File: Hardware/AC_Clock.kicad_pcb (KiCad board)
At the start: 2 copper layers, 132.1 x 100.3 mm, 71 parts, among them J1 L, J2 N, J3 Conn_01x10, J4 Conn_01x10, J5 Conn_01x10, J6 Conn_01x10, SW1 Min_PB, SW2 Hr_PB, T1 10:1, U1 AZ1117-5.0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

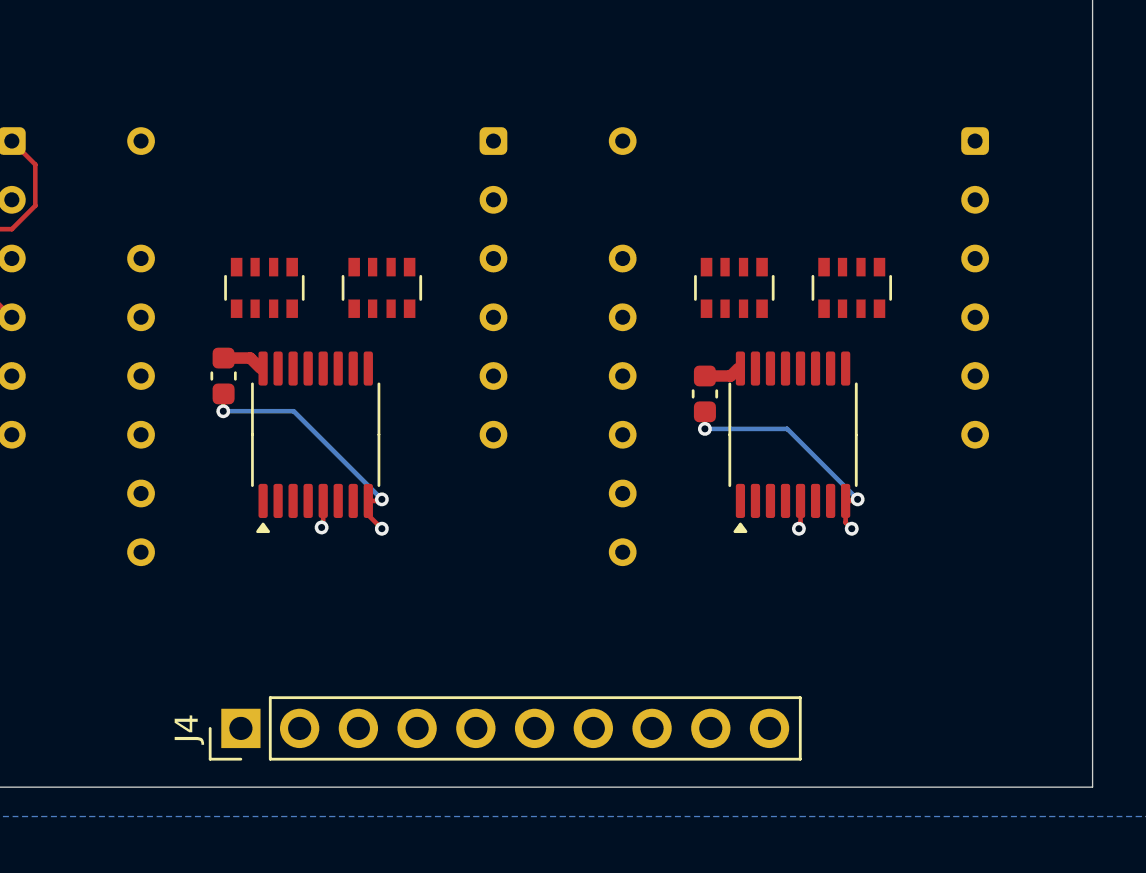
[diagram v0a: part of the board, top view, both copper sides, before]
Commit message: Route the 10/hours digits. Update HDSP-816E footprint to include 3D representation
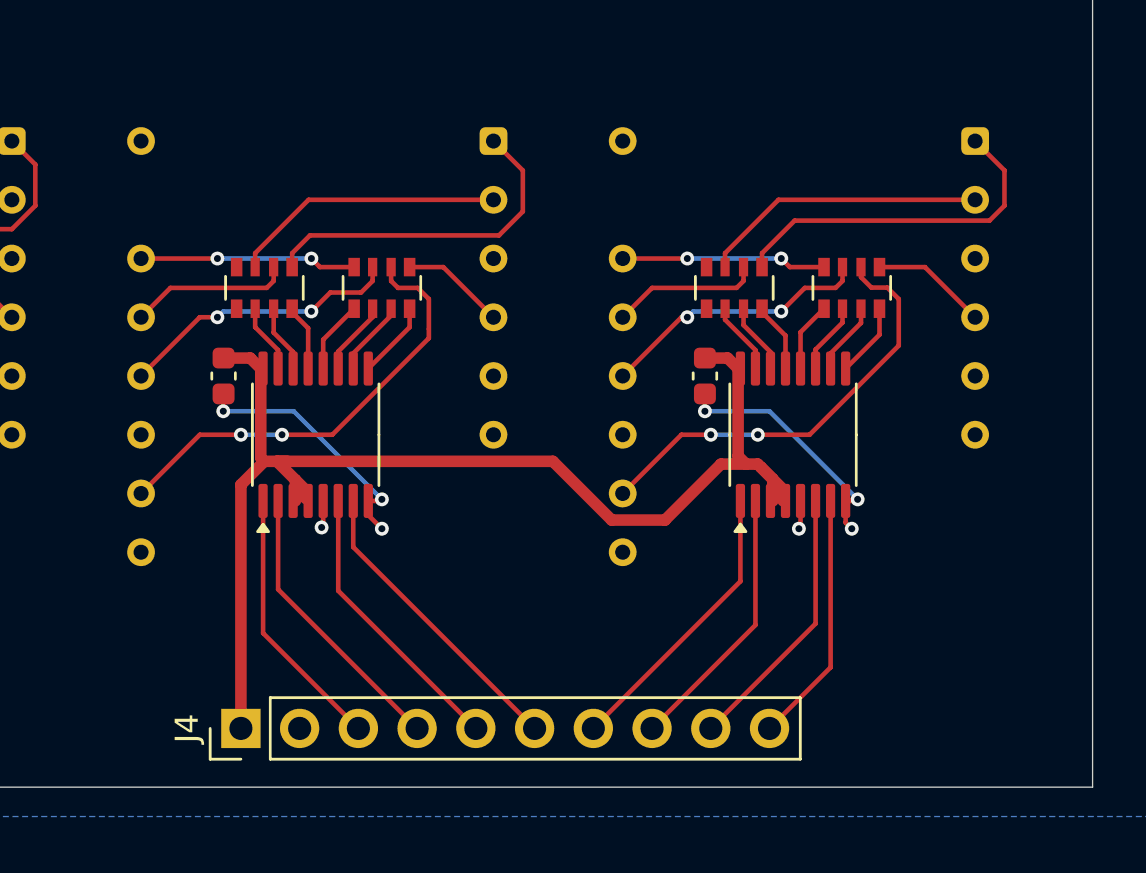
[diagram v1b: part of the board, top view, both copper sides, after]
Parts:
- moved C9 0.78 mm to (148.3, 64.8)
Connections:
- RN7 pad 2: unconnected-(RN7B-R2.1-Pad2) -> Net-(RN7B-R2.1)
- U12 pad 15: unconnected-(U12-Qf-Pad15) -> Net-(RN7B-R2.1)
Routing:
- net +5V: track 204.1 -> 255.1 mm
- net Net-(RN6-R3.2): track 0.00 -> 19.5 mm, vias 0 -> 2
- net Net-(RN8-R3.2): track 0.00 -> 19.1 mm, vias 0 -> 2
- net Net-(RN7D-R4.2): track 0.00 -> 15.3 mm
- net Net-(RN5D-R4.2): track 0.00 -> 14.9 mm
- net DA_3: track 6.38 -> 19.5 mm
- net DB_4: track 0.00 -> 12.5 mm
- net Net-(RN7B-R2.2): track 0.00 -> 12.4 mm
- net DC_3: track 0.00 -> 12.3 mm
- net Net-(RN6-R2.2): track 0.00 -> 12.3 mm, vias 0 -> 2
- net DD_3: track 3.12 -> 15.4 mm
- net Net-(RN5B-R2.2): track 0.00 -> 11.9 mm
- net Net-(RN8-R2.2): track 0.00 -> 11.8 mm, vias 0 -> 2
- net DD_4: track 0.00 -> 11.7 mm
- net DC_4: track 0.00 -> 11.7 mm
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
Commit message: Finish routing main board
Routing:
- net +5V: track 255.1 -> 319.2 mm, vias 2 -> 4
- net DB_3: track 11.5 -> 54.6 mm, vias 0 -> 1
- net DB_1: track 11.4 -> 48.1 mm, vias 0 -> 1
- net DC_3: track 12.3 -> 48.1 mm, vias 0 -> 1
- net DD_3: track 15.4 -> 49.1 mm, vias 0 -> 1
- net DC_1: track 12.2 -> 45.5 mm, vias 0 -> 1
- net DD_1: track 15.3 -> 45.4 mm, vias 0 -> 1
- net DA_3: track 19.5 -> 48.6 mm, vias 0 -> 1
- net /hour: track 9.21 -> 35.2 mm
- net /RST_{10hr}: track 0.00 -> 20.3 mm
- net DA_1: track 19.3 -> 39.6 mm, vias 0 -> 1
- net DA_2: track 14.8 -> 30.0 mm
- net DB_4: track 12.5 -> 26.7 mm
- net DB_2: track 12.7 -> 26.2 mm, vias 0 -> 1
- net DD_4: track 11.7 -> 24.9 mm
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
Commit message: Add Class Y Safety capacitor
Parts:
- added C10: Safety, Capacitor_THT:C_Disc_D7.5mm_W5.0mm_P7.50mm, F.Cu at (59.8, 109.7)
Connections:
- D5 pad 1: /4Hz -> /2Hz
- T1 pad 10: (no net) -> unconnected-(T1-Pad10)
- T1 pad 9: (no net) -> unconnected-(T1-Pad9)
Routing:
- net /AC_12-: track 14.7 -> 26.6 mm
- net Earth: track 50.4 -> 56.1 mm

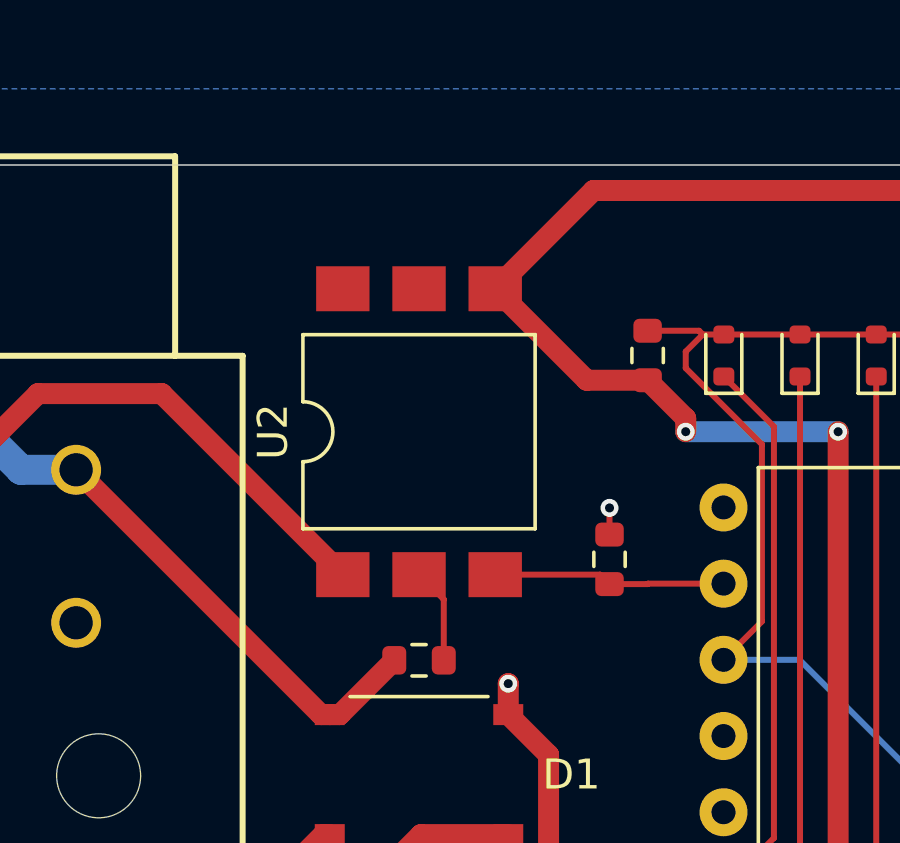
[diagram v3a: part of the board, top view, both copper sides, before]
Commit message: Fix U2 footprint; change to DIP-4
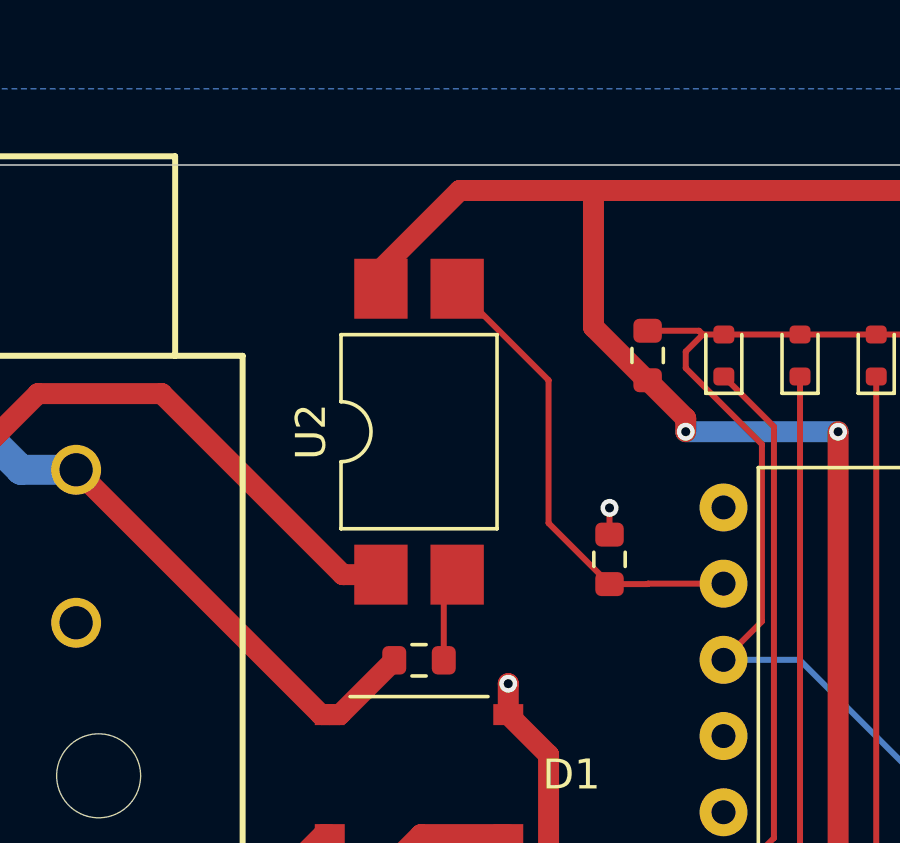
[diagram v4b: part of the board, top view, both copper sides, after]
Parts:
- U2: footprint Package_DIP:SMDIP-6_W9.53mm_Clearance8mm -> Package_DIP:SMDIP-4_W9.53mm
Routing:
- net /Pulse: track 7.75 -> 15.8 mm
- net +5V: track 319.2 -> 324.1 mm
- net /AC_12+: track 50.8 -> 52.1 mm
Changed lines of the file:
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@@
 		)
 	)
-	(footprint "Package_DIP:SMDIP-6_W9.53mm_Clearance8mm"
+	(footprint "Package_DIP:SMDIP-4_W9.53mm"
 		(layer "F.Cu")
 		(at 87.63 115.57 90)
-		(descr "6-lead surface-mounted (SMD) DIP package, row spacing 9.53 mm (375 mils), Clearance8mm")
-		(tags "SMD DIP DIL PDIP SMDIP 2.54mm 9.53mm 375mil Clearance8mm")
+		(descr "4-lead surface-mounted (SMD) DIP package, row spacing 9.53 mm (375 mils)")
+		(tags "SMD DIP DIL PDIP SMDIP 2.54mm 9.53mm 375mil")
 		(property "Reference" "U2"
-			(at 0 -4.87 90)
+			(at 0 -3.6 90)
 			(layer "F.SilkS")
 			(effects
@@
 		)
 		(property "Value" "LTV-817S"
-			(at 0 4.87 90)
+			(at 0 3.6 90)
 			(layer "F.Fab")
 			(effects
@@
 			)
 		)
-		(property "Footprint" "Package_DIP:SMDIP-6_W9.53mm_Clearance8mm"
+		(property "Footprint" "Package_DIP:SMDIP-4_W9.53mm"
 			(at 0 0 90)
 			(unlocked yes)
@@
 		(attr smd)
 		(fp_line
-			(start 3.235 -3.87)
-			(end 1 -3.87)
+			(start 3.235 -2.6)
+			(end 1 -2.6)
 			(stroke
 				(width 0.12)
@@
 		)
 		(fp_line
-			(start -1 -3.87)
-			(end -3.235 -3.87)
+			(start -1 -2.6)
+			(end -3.235 -2.6)
 			(stroke
 				(width 0.12)
@@
 		)
 		(fp_line
-			(start -3.235 -3.87)
-			(end -3.235 3.87)
+			(start -3.235 -2.6)
+			(end -3.235 2.6)
 			(stroke
 				(width 0.12)
@@
 		)
 		(fp_line
-			(start 3.235 3.87)
-			(end 3.235 -3.87)
+			(start 3.235 2.6)
+			(end 3.235 -2.6)
 			(stroke
 				(width 0.12)
@@
 		)
 		(fp_line
-			(start -3.235 3.87)
-			(end 3.235 3.87)
+			(start -3.235 2.6)
+			(end 3.235 2.6)
 			(stroke
 				(width 0.12)
@@
 		)
 		(fp_arc
-			(start 1 -3.87)
-			(mid 0 -2.87)
-			(end -1 -3.87)
+			(start 1 -2.6)
+			(mid 0 -1.6)
+			(end -1 -2.6)
 			(stroke
 				(width 0.12)
@@
 		)
 		(fp_line
-			(start 5.8 -4.1)
-			(end -5.8 -4.1)
+			(start 6.05 -2.8)
+			(end -6.05 -2.8)
 			(stroke
 				(width 0.05)
@@
 		)
 		(fp_line
-			(start -5.8 -4.1)
-			(end -5.8 4.1)
+			(start -6.05 -2.8)
+			(end -6.05 2.8)
 			(stroke
 				(width 0.05)
@@
 		)
 		(fp_line
-			(start 5.8 4.1)
-			(end 5.8 -4.1)
+			(start 6.05 2.8)
+			(end 6.05 -2.8)
 			(stroke
 				(width 0.05)
@@
 		)
 		(fp_line
-			(start -5.8 4.1)
-			(end 5.8 4.1)
+			(start -6.05 2.8)
+			(end 6.05 2.8)
 			(stroke
 				(width 0.05)
@@
 		)
 		(fp_line
-			(start 3.175 -3.81)
-			(end 3.175 3.81)
+			(start 3.175 -2.54)
+			(end 3.175 2.54)
 			(stroke
 				(width 0.1)
@@
 		)
 		(fp_line
-			(start -2.175 -3.81)
-			(end 3.175 -3.81)
+			(start -2.175 -2.54)
+			(end 3.175 -2.54)
 			(stroke
 				(width 0.1)
@@
 		)
 		(fp_line
-			(start -3.175 -2.81)
-			(end -2.175 -3.81)
+			(start -3.175 -1.54)
+			(end -2.175 -2.54)
 			(stroke
 				(width 0.1)
@@
 		)
 		(fp_line
-			(start 3.175 3.81)
-			(end -3.175 3.81)
+			(start 3.175 2.54)
+			(end -3.175 2.54)
 			(stroke
 				(width 0.1)
@@
 		)
 		(fp_line
-			(start -3.175 3.81)
-			(end -3.175 -2.81)
+			(start -3.175 2.54)
+			(end -3.175 -1.54)
 			(stroke
 				(width 0.1)
@@
 		)
 		(pad "1" smd rect
-			(at -4.765 -2.54 90)
-			(size 1.5 1.78)
+			(at -4.765 -1.27 90)
+			(size 2 1.78)
 			(layers "F.Cu" "F.Paste" "F.Mask")
 			(net 4 "/AC_12+")
@@
 		)
 		(pad "2" smd rect
-			(at -4.765 0 90)
-			(size 1.5 1.78)
+			(at -4.765 1.27 90)
+			(size 2 1.78)
 			(layers "F.Cu" "F.Paste" "F.Mask")
 			(net 27 "Net-(R1-Pad2)")
@@
 		)
 		(pad "3" smd rect
-			(at -4.765 2.54 90)
-			(size 1.5 1.78)
+			(at 4.765 1.27 90)
+			(size 2 1.78)
 			(layers "F.Cu" "F.Paste" "F.Mask")
 			(net 28 "/Pulse")
@@
 		)
 		(pad "4" smd rect
-			(at 4.765 2.54 90)
-			(size 1.5 1.78)
+			(at 4.765 -1.27 90)
+			(size 2 1.78)
 			(layers "F.Cu" "F.Paste" "F.Mask")
 			(net 3 "+5V")
 			(pintype "passive")
 		)
-		(pad "5" smd rect
-			(at 4.765 0 90)
-			(size 1.5 1.78)
-			(layers "F.Cu" "F.Paste" "F.Mask")
-		)
-		(pad "6" smd rect
-			(at 4.765 -2.54 90)
-			(size 1.5 1.78)
-			(layers "F.Cu" "F.Paste" "F.Mask")
-		)
-		(model "${KICAD8_3DMODEL_DIR}/Package_DIP.3dshapes/SMDIP-6_W9.53mm.wrl"
+		(model "${KICAD8_3DMODEL_DIR}/Package_DIP.3dshapes/SMDIP-4_W9.53mm.wrl"
 			(offset
 				(xyz 0 0 0)
@@
 	)
 	(segment
-		(start 93.22 113.855)
-		(end 90.17 110.805)
-		(width 0.7)
-		(layer "F.Cu")
-		(net 3)
-	)
-	(segment
 		(start 151.721 69.679)
 		(end 151.721 70.1725)
@@
 	)
 	(segment
+		(start 95.25 113.855)
+		(end 95.217376 113.855)
+		(width 0.7)
+		(layer "F.Cu")
+		(net 3)
+	)
+	(segment
 		(start 151.13 133.795)
 		(end 152.005 134.67)
@@
 	)
 	(segment
+		(start 86.36 110.805)
+		(end 86.36 110.155)
+		(width 0.7)
+		(layer "F.Cu")
+		(net 3)
+	)
+	(segment
 		(start 87.63 141.58)
 		(end 90.285 138.925)
@@
 	)
 	(segment
+		(start 88.985 107.53)
+		(end 93.445 107.53)
+		(width 0.7)
+		(layer "F.Cu")
+		(net 3)
+	)
+	(segment
 		(start 119.38 118.555)
 		(end 108.516 118.555)
@@
 	)
 	(segment
-		(start 95.25 113.855)
-		(end 93.22 113.855)
-		(width 0.7)
-		(layer "F.Cu")
-		(net 3)
-	)
-	(segment
 		(start 150.622 68.58)
 		(end 150.749 68.707)
@@
 	)
 	(segment
+		(start 93.445 112.082624)
+		(end 93.445 107.53)
+		(width 0.7)
+		(layer "F.Cu")
+		(net 3)
+	)
+	(segment
 		(start 107.696 68.58)
 		(end 108.369 67.907)
@@
 	)
 	(segment
-		(start 90.17 110.805)
-		(end 93.445 107.53)
+		(start 86.36 110.155)
+		(end 88.985 107.53)
 		(width 0.7)
 		(layer "F.Cu")
@@
 	)
 	(segment
+		(start 95.217376 113.855)
+		(end 93.445 112.082624)
+		(width 0.7)
+		(layer "F.Cu")
+		(net 3)
+	)
+	(segment
 		(start 148.336 63.995)
 		(end 149.3185 63.995)
@@
 	)
 	(segment
-		(start 76.2 137.24)
-		(end 75.01 137.24)
+		(start 79.055 114.3)
+		(end 85.09 120.335)
 		(width 0.7)
 		(layer "F.Cu")
@@
 	)
 	(segment
-		(start 72.39 134.62)
-		(end 72.39 116.84)
+		(start 76.2 137.24)
+		(end 75.01 137.24)
 		(width 0.7)
 		(layer "F.Cu")
@@
 	)
 	(segment
+		(start 72.39 134.62)
+		(end 72.39 116.84)
+		(width 0.7)
+		(layer "F.Cu")
+		(net 4)
+	)
+	(segment
 		(start 72.39 116.84)
 		(end 74.93 114.3)
@@
 	)
 	(segment
-		(start 79.055 114.3)
-		(end 85.09 120.335)
+		(start 85.09 120.335)
+		(end 86.36 120.335)
 		(width 0.7)
 		(layer "F.Cu")
@@
 	)
 	(segment
-		(start 88.455 121.16)
+		(start 88.455 120.78)
 		(end 88.455 123.19)
 		(width 0.2)
@@
 	)
 	(segment
-		(start 87.63 120.335)
-		(end 88.455 121.16)
+		(start 88.9 120.335)
+		(end 88.455 120.78)
 		(width 0.2)
 		(layer "F.Cu")
@@
 	)
 	(segment
-		(start 90.17 120.335)
-		(end 93.665 120.335)
+		(start 91.948 118.618)
+		(end 93.98 120.65)
 		(width 0.2)
 		(layer "F.Cu")
@@
 	)
 	(segment
-		(start 93.665 120.335)
-		(end 93.98 120.65)
+		(start 91.948 113.853)
+		(end 91.948 118.618)
+		(width 0.2)
+		(layer "F.Cu")
+		(net 28)
+	)
+	(segment
+		(start 88.9 110.805)
+		(end 91.948 113.853)
 		(width 0.2)
 		(layer "F.Cu")
